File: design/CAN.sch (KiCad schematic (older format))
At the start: 4 parts, among them U401 SN65HVD232

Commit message: Saved project with more recent version of KiCad. Added IRS2184 half bridge driver to BLDC_4_cache.lib
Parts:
- C401: symbol C -> C-RESCUE-BLDC_4
- R401, R402: symbol R -> R-RESCUE-BLDC_4
- U401: symbol MCP2551-I/SN -> MCP2551-I/SN-RESCUE-BLDC_4
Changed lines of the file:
@@
 EESchema Schematic File Version 2
+LIBS:BLDC_4-rescue
 LIBS:power
 LIBS:device
@@
 LIBS:crf_1
 LIBS:BLDC_4-cache
-EELAYER 24 0
+EELAYER 25 0
 EELAYER END
 $Descr A4 11693 8268
@@
 $EndDescr
 $Comp
-L MCP2551-I/SN U401
+L MCP2551-I/SN-RESCUE-BLDC_4 U401
 U 1 1 53F59F90
 P 5850 4050
@@
 $EndComp
 $Comp
-L GND #PWR025
+L GND-RESCUE-BLDC_4 #PWR025
 U 1 1 53F59F97
 P 5850 4450
@@
 $EndComp
 $Comp
-L C C401
+L C-RESCUE-BLDC_4 C401
 U 1 1 53F59FA3
 P 6150 3400
@@
 $EndComp
 $Comp
-L GND #PWR028
+L GND-RESCUE-BLDC_4 #PWR028
 U 1 1 53F59FB0
 P 6150 3600
@@
 CAN_TX
 $Comp
-L R R401
+L R-RESCUE-BLDC_4 R401
 U 1 1 540030A8
 P 4900 4050
@@
 NoConn ~ 6300 4100
 $Comp
-L R R402
+L R-RESCUE-BLDC_4 R402
 U 1 1 54003136
 P 6400 4600
@@
 	6400 4250 6300 4250
 $Comp
-L GND #PWR029
+L GND-RESCUE-BLDC_4 #PWR029
 U 1 1 5400318B
 P 6400 4850

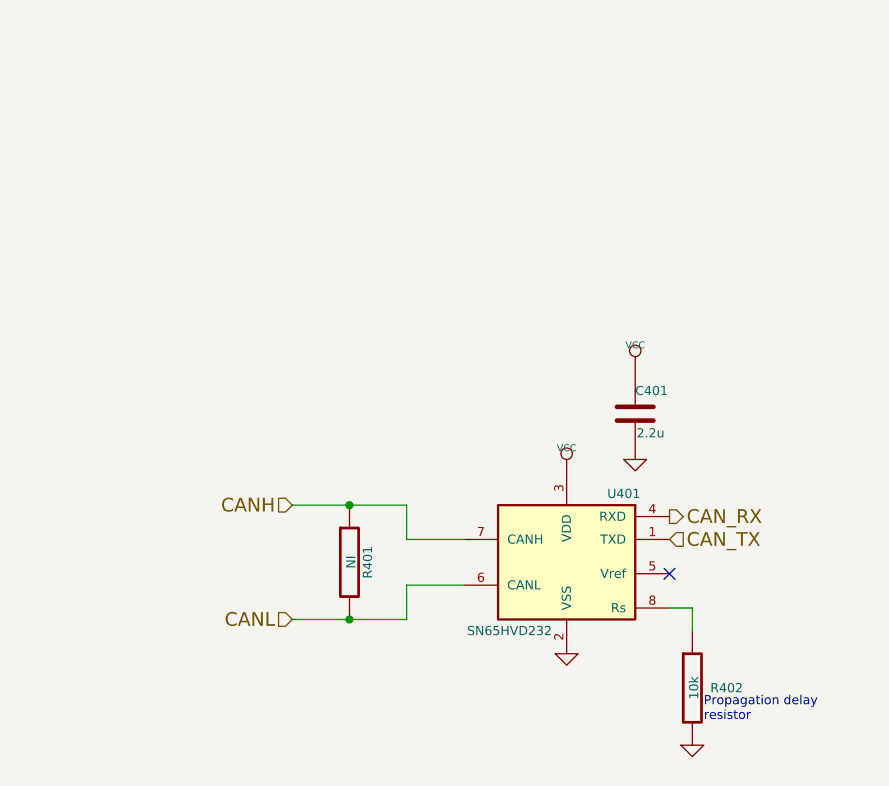
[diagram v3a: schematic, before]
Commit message: Removed 5V power level. Integrated isolated CAN bus driver.
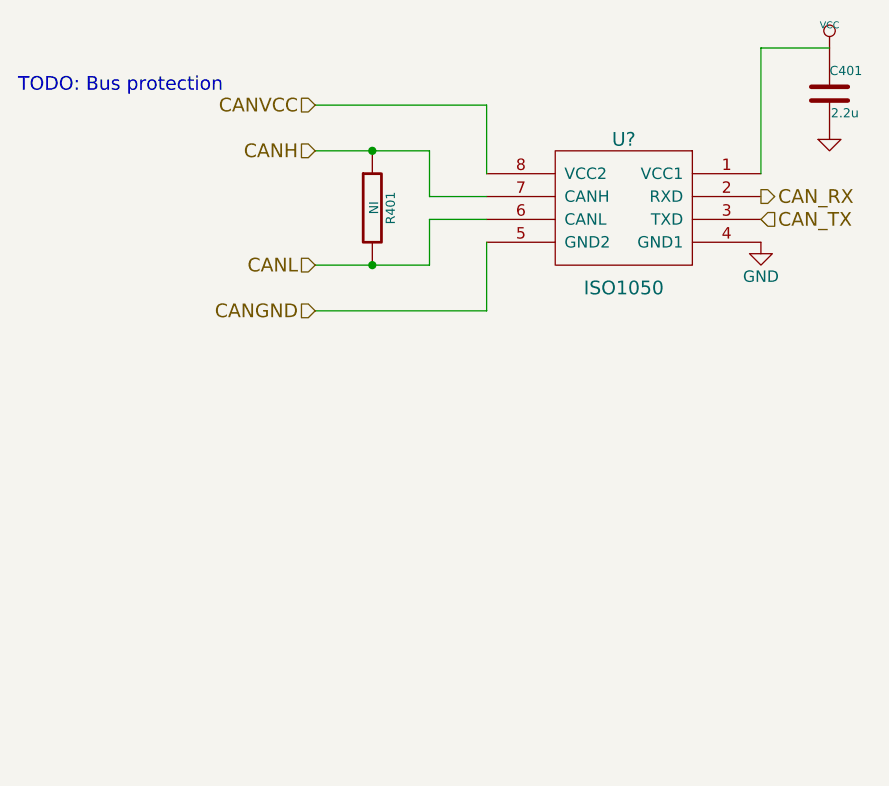
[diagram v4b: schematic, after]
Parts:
- removed R402: 10k, SMD_Packages:SMD-0603_r, symbol R-RESCUE-BLDC_4
- removed U401: SN65HVD232, SMD_Packages:SOIC-8-W, symbol MCP2551-I/SN-RESCUE-BLDC_4
- added U?: ISO1050, symbol ISO1050
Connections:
- net CANH: now also U?.7 (CANH)
- net CANL: now also U?.6 (CANL)
- net CAN_RX: now also U?.2 (RXD)
- net CAN_TX: now also U?.3 (TXD)
- net GND: now also U?.4 (GND1)
- net VCC: now also U?.1 (VCC1)
- new net CANGND: U?.5 (GND2)
- new net CANVCC: U?.8 (VCC2)
- no-connect marks 1 -> 0
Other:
- note added: "TODO: Bus protection"
- note removed: "Propagation delay\nresistor"
- moved on the sheet: C401, R401
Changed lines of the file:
@@
 $Descr A4 11693 8268
 encoding utf-8
-Sheet 4 10
+Sheet 3 10
 Title "CAN BUS transceiver"
-Date "25 Aug 2014"
+Date "2015-08-27"
 Rev ""
-Comp "Mrk Industries"
+Comp "Jörg Wangemann"
 Comment1 ""
 Comment2 ""
@@
 $EndDescr
 $Comp
-L MCP2551-I/SN-RESCUE-BLDC_4 U401
-U 1 1 53F59F90
-P 5850 4050
-F 0 "U401" H 5600 4350 40  0000 C CNN
-F 1 "SN65HVD232" H 6100 3750 40  0000 C CNN
-F 2 "SMD_Packages:SOIC-8-W" H 5850 4050 35  0001 C CIN
-F 3 "" H 5850 4050 60  0000 C CNN
-	1    5850 4050
-	-1   0    0    -1
-$EndComp
-$Comp
-L GND-RESCUE-BLDC_4 #PWR025
-U 1 1 53F59F97
-P 5850 4450
-F 0 "#PWR025" H 5850 4450 30  0001 C CNN
-F 1 "GND" H 5850 4380 30  0001 C CNN
-F 2 "" H 5850 4450 60  0000 C CNN
-F 3 "" H 5850 4450 60  0000 C CNN
-	1    5850 4450
-	1    0    0    -1
-$EndComp
-$Comp
-L VCC #PWR026
-U 1 1 53F59F9D
-P 5850 3650
-F 0 "#PWR026" H 5850 3750 30  0001 C CNN
-F 1 "VCC" H 5850 3750 30  0000 C CNN
-F 2 "" H 5850 3650 60  0001 C CNN
-F 3 "" H 5850 3650 60  0001 C CNN
-	1    5850 3650
-	1    0    0    -1
-$EndComp
-$Comp
 L C-RESCUE-BLDC_4 C401
 U 1 1 53F59FA3
-P 6150 3400
-F 0 "C401" H 6150 3500 40  0000 L CNN
-F 1 "2.2u" H 6156 3315 40  0000 L CNN
-F 2 "SMD_Packages:SMD-0402" H 6188 3250 30  0001 C CNN
-F 3 "" H 6150 3400 60  0000 C CNN
-	1    6150 3400
+P 7000 2000
+F 0 "C401" H 7000 2100 40  0000 L CNN
+F 1 "2.2u" H 7006 1915 40  0000 L CNN
+F 2 "SMD_Packages:SMD-0402" H 7038 1850 30  0001 C CNN
+F 3 "" H 7000 2000 60  0000 C CNN
+	1    7000 2000
 	1    0    0    -1
 $EndComp
@@
 L VCC #PWR027
 U 1 1 53F59FAA
-P 6150 3200
-F 0 "#PWR027" H 6150 3300 30  0001 C CNN
-F 1 "VCC" H 6150 3300 30  0000 C CNN
-F 2 "" H 6150 3200 60  0001 C CNN
-F 3 "" H 6150 3200 60  0001 C CNN
-	1    6150 3200
+P 7000 1800
+F 0 "#PWR027" H 7000 1900 30  0001 C CNN
+F 1 "VCC" H 7000 1900 30  0000 C CNN
+F 2 "" H 7000 1800 60  0001 C CNN
+F 3 "" H 7000 1800 60  0001 C CNN
+	1    7000 1800
 	1    0    0    -1
 $EndComp
@@
 L GND-RESCUE-BLDC_4 #PWR028
 U 1 1 53F59FB0
-P 6150 3600
-F 0 "#PWR028" H 6150 3600 30  0001 C CNN
-F 1 "GND" H 6150 3530 30  0001 C CNN
-F 2 "" H 6150 3600 60  0000 C CNN
-F 3 "" H 6150 3600 60  0000 C CNN
-	1    6150 3600
+P 7000 2200
+F 0 "#PWR028" H 7000 2200 30  0001 C CNN
+F 1 "GND-RESCUE-BLDC_4" H 7000 2130 30  0001 C CNN
+F 2 "" H 7000 2200 60  0000 C CNN
+F 3 "" H 7000 2200 60  0000 C CNN
+	1    7000 2200
 	1    0    0    -1
 $EndComp
@@
 EndData
 $EndBitmap
-Text HLabel 6300 3850 2    60   Output ~ 0
+Text HLabel 6700 2450 2    60   Output ~ 0
 CAN_RX
-Text HLabel 6300 3950 2    60   Input ~ 0
+Text HLabel 6700 2550 2    60   Input ~ 0
 CAN_TX
 $Comp
 L R-RESCUE-BLDC_4 R401
 U 1 1 540030A8
-P 4900 4050
-F 0 "R401" V 4980 4050 40  0000 C CNN
-F 1 "NI" V 4907 4051 40  0000 C CNN
-F 2 "SMD_Packages:SMD-0603_r" V 4830 4050 30  0001 C CNN
-F 3 "" H 4900 4050 30  0000 C CNN
-	1    4900 4050
+P 5000 2500
+F 0 "R401" V 5080 2500 40  0000 C CNN
+F 1 "NI" V 5007 2501 40  0000 C CNN
+F 2 "SMD_Packages:SMD-0603_r" V 4930 2500 30  0001 C CNN
+F 3 "" H 5000 2500 30  0000 C CNN
+	1    5000 2500
 	1    0    0    -1
 $EndComp
-Text HLabel 4650 3800 0    60   Input ~ 0
+Text HLabel 4750 2250 0    60   Input ~ 0
 CANH
-Text HLabel 4650 4300 0    60   Input ~ 0
+Text HLabel 4750 2750 0    60   Input ~ 0
 CANL
 Wire Wire Line
-	4650 4300 5150 4300
+	5250 2750 4750 2750
 Wire Wire Line
-	5150 4300 5150 4150
+	5250 2550 5250 2750
+Connection ~ 5000 2750
 Wire Wire Line
-	5150 4150 5400 4150
-Connection ~ 4900 4300
+	5250 2250 5250 2450
 Wire Wire Line
-	5400 3950 5150 3950
+	5250 2250 4750 2250
+Connection ~ 5000 2250
+$Comp
+L ISO1050 U?
+U 1 1 55E64568
+P 6100 2500
+F 0 "U?" H 6100 2800 60  0000 C CNN
+F 1 "ISO1050" H 6100 2150 60  0000 C CNN
+F 2 "" H 6100 2500 60  0000 C CNN
+F 3 "" H 6100 2500 60  0000 C CNN
+	1    6100 2500
+	-1   0    0    -1
+$EndComp
+Text Notes 3450 2000 0    60   ~ 0
+TODO: Bus protection
 Wire Wire Line
-	5150 3950 5150 3800
+	6700 2350 6700 1800
 Wire Wire Line
-	5150 3800 4650 3800
-Connection ~ 4900 3800
-NoConn ~ 6300 4100
+	6700 1800 7000 1800
 $Comp
-L R-RESCUE-BLDC_4 R402
-U 1 1 54003136
-P 6400 4600
-F 0 "R402" H 6550 4600 40  0000 C CNN
-F 1 "10k" V 6407 4601 40  0000 C CNN
-F 2 "SMD_Packages:SMD-0603_r" V 6330 4600 30  0001 C CNN
-F 3 "" H 6400 4600 30  0000 C CNN
-	1    6400 4600
+L GND #PWR?
+U 1 1 55E64902
+P 6700 2650
+F 0 "#PWR?" H 6700 2400 50  0001 C CNN
+F 1 "GND" H 6700 2500 50  0000 C CNN
+F 2 "" H 6700 2650 60  0000 C CNN
+F 3 "" H 6700 2650 60  0000 C CNN
+	1    6700 2650
 	1    0    0    -1
 $EndComp
 Wire Wire Line
-	6400 4350 6400 4250
+	5250 2450 5500 2450
 Wire Wire Line
-	6400 4250 6300 4250
-$Comp
-L GND-RESCUE-BLDC_4 #PWR029
-U 1 1 5400318B
-P 6400 4850
-F 0 "#PWR029" H 6400 4850 30  0001 C CNN
-F 1 "GND" H 6400 4780 30  0001 C CNN
-F 2 "" H 6400 4850 60  0000 C CNN
-F 3 "" H 6400 4850 60  0000 C CNN
-	1    6400 4850
-	1    0    0    -1
-$EndComp
-Text Notes 6450 4750 0    40   ~ 0
-Propagation delay\nresistor
+	5500 2550 5250 2550
+Text HLabel 4750 2950 0    60   Input ~ 0
+CANGND
+Text HLabel 4750 2050 0    60   Input ~ 0
+CANVCC
+Wire Wire Line
+	4750 2050 5500 2050
+Wire Wire Line
+	5500 2050 5500 2350
+Wire Wire Line
+	4750 2950 5500 2950
+Wire Wire Line
+	5500 2950 5500 2650
 $EndSCHEMATC

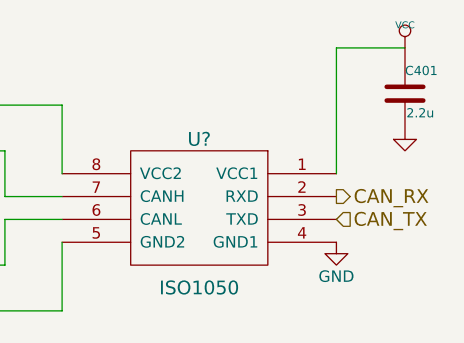
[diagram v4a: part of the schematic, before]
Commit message: First complete draft of the schematics.
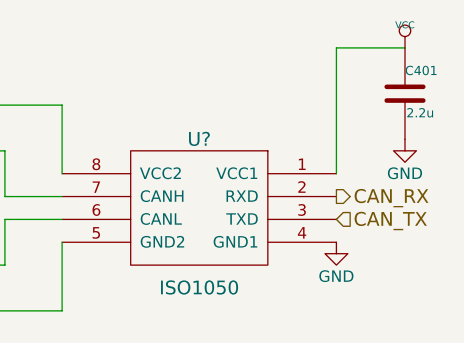
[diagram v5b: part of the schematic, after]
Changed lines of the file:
@@
 $Descr A4 11693 8268
 encoding utf-8
-Sheet 3 10
+Sheet 3 11
 Title "CAN BUS transceiver"
 Date "2015-08-27"
@@
 F 3 "" H 7000 1800 60  0001 C CNN
 	1    7000 1800
-	1    0    0    -1
-$EndComp
-$Comp
-L GND-RESCUE-BLDC_4 #PWR028
-U 1 1 53F59FB0
-P 7000 2200
-F 0 "#PWR028" H 7000 2200 30  0001 C CNN
-F 1 "GND-RESCUE-BLDC_4" H 7000 2130 30  0001 C CNN
-F 2 "" H 7000 2200 60  0000 C CNN
-F 3 "" H 7000 2200 60  0000 C CNN
-	1    7000 2200
 	1    0    0    -1
 $EndComp
@@
 Wire Wire Line
 	5500 2950 5500 2650
+$Comp
+L GND #PWR?
+U 1 1 55E749EE
+P 7000 2200
+F 0 "#PWR?" H 7000 1950 50  0001 C CNN
+F 1 "GND" H 7000 2050 50  0000 C CNN
+F 2 "" H 7000 2200 60  0000 C CNN
+F 3 "" H 7000 2200 60  0000 C CNN
+	1    7000 2200
+	1    0    0    -1
+$EndComp
 $EndSCHEMATC

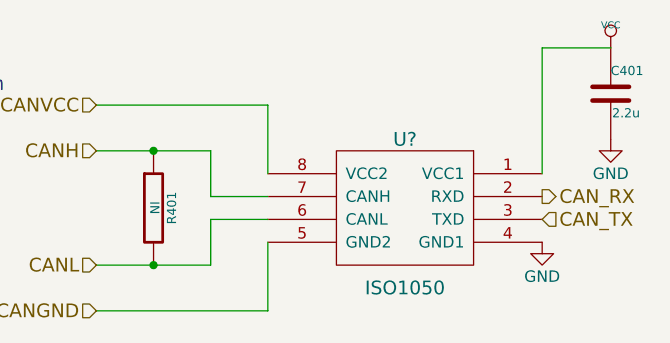
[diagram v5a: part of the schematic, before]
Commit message: Assigned some footprints.
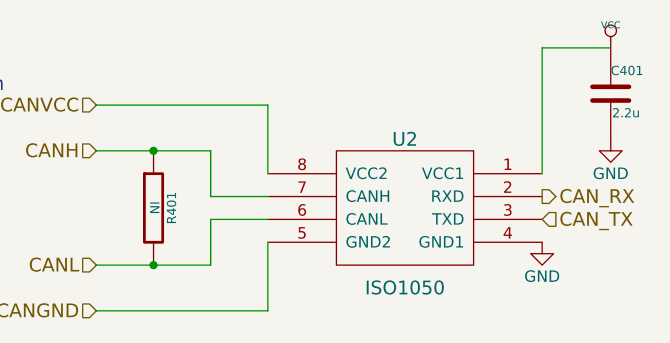
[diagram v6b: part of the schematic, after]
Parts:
- C401: footprint SMD_Packages:SMD-0402 -> Capacitors_SMD:C_0603
- gave numbers to parts that had none: 1
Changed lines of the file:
@@
 F 0 "C401" H 7000 2100 40  0000 L CNN
 F 1 "2.2u" H 7006 1915 40  0000 L CNN
-F 2 "SMD_Packages:SMD-0402" H 7038 1850 30  0001 C CNN
+F 2 "Capacitors_SMD:C_0603" H 7038 1850 30  0001 C CNN
 F 3 "" H 7000 2000 60  0000 C CNN
 	1    7000 2000
@@
 $EndComp
 $Comp
-L VCC #PWR027
+L VCC #PWR022
 U 1 1 53F59FAA
 P 7000 1800
-F 0 "#PWR027" H 7000 1900 30  0001 C CNN
+F 0 "#PWR022" H 7000 1900 30  0001 C CNN
 F 1 "VCC" H 7000 1900 30  0000 C CNN
 F 2 "" H 7000 1800 60  0001 C CNN
@@
 Connection ~ 5000 2250
 $Comp
-L ISO1050 U?
+L ISO1050 U2
 U 1 1 55E64568
 P 6100 2500
-F 0 "U?" H 6100 2800 60  0000 C CNN
+F 0 "U2" H 6100 2800 60  0000 C CNN
 F 1 "ISO1050" H 6100 2150 60  0000 C CNN
-F 2 "" H 6100 2500 60  0000 C CNN
+F 2 "" H 6100 2500 60  0001 C CNN
 F 3 "" H 6100 2500 60  0000 C CNN
 	1    6100 2500
@@
 	6700 1800 7000 1800
 $Comp
-L GND #PWR?
+L GND #PWR023
 U 1 1 55E64902
 P 6700 2650
-F 0 "#PWR?" H 6700 2400 50  0001 C CNN
+F 0 "#PWR023" H 6700 2400 50  0001 C CNN
 F 1 "GND" H 6700 2500 50  0000 C CNN
 F 2 "" H 6700 2650 60  0000 C CNN
@@
 	5500 2950 5500 2650
 $Comp
-L GND #PWR?
+L GND #PWR024
 U 1 1 55E749EE
 P 7000 2200
-F 0 "#PWR?" H 7000 1950 50  0001 C CNN
+F 0 "#PWR024" H 7000 1950 50  0001 C CNN
 F 1 "GND" H 7000 2050 50  0000 C CNN
 F 2 "" H 7000 2200 60  0000 C CNN

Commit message: Selected footprints
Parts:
- R401: footprint SMD_Packages:SMD-0603_r -> Resistors_SMD:R_0603_HandSoldering
- U2: footprint (none) -> CRF1:PDSO-G8
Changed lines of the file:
@@
 F 0 "R401" V 5080 2500 40  0000 C CNN
 F 1 "NI" V 5007 2501 40  0000 C CNN
-F 2 "SMD_Packages:SMD-0603_r" V 4930 2500 30  0001 C CNN
+F 2 "Resistors_SMD:R_0603_HandSoldering" V 4930 2500 30  0001 C CNN
 F 3 "" H 5000 2500 30  0000 C CNN
 	1    5000 2500
@@
 F 0 "U2" H 6100 2800 60  0000 C CNN
 F 1 "ISO1050" H 6100 2150 60  0000 C CNN
-F 2 "" H 6100 2500 60  0001 C CNN
+F 2 "CRF1:PDSO-G8" H 6100 2500 60  0001 C CNN
 F 3 "" H 6100 2500 60  0000 C CNN
 	1    6100 2500
